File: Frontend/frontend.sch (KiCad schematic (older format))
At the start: 13 parts, among them J1 VOCM, J2 BNC, J3 UMC, J4 UMC, J5 VOCM, J6 BNC, J7 UMC, J8 UMC, J9 PCIEx4 EDGE

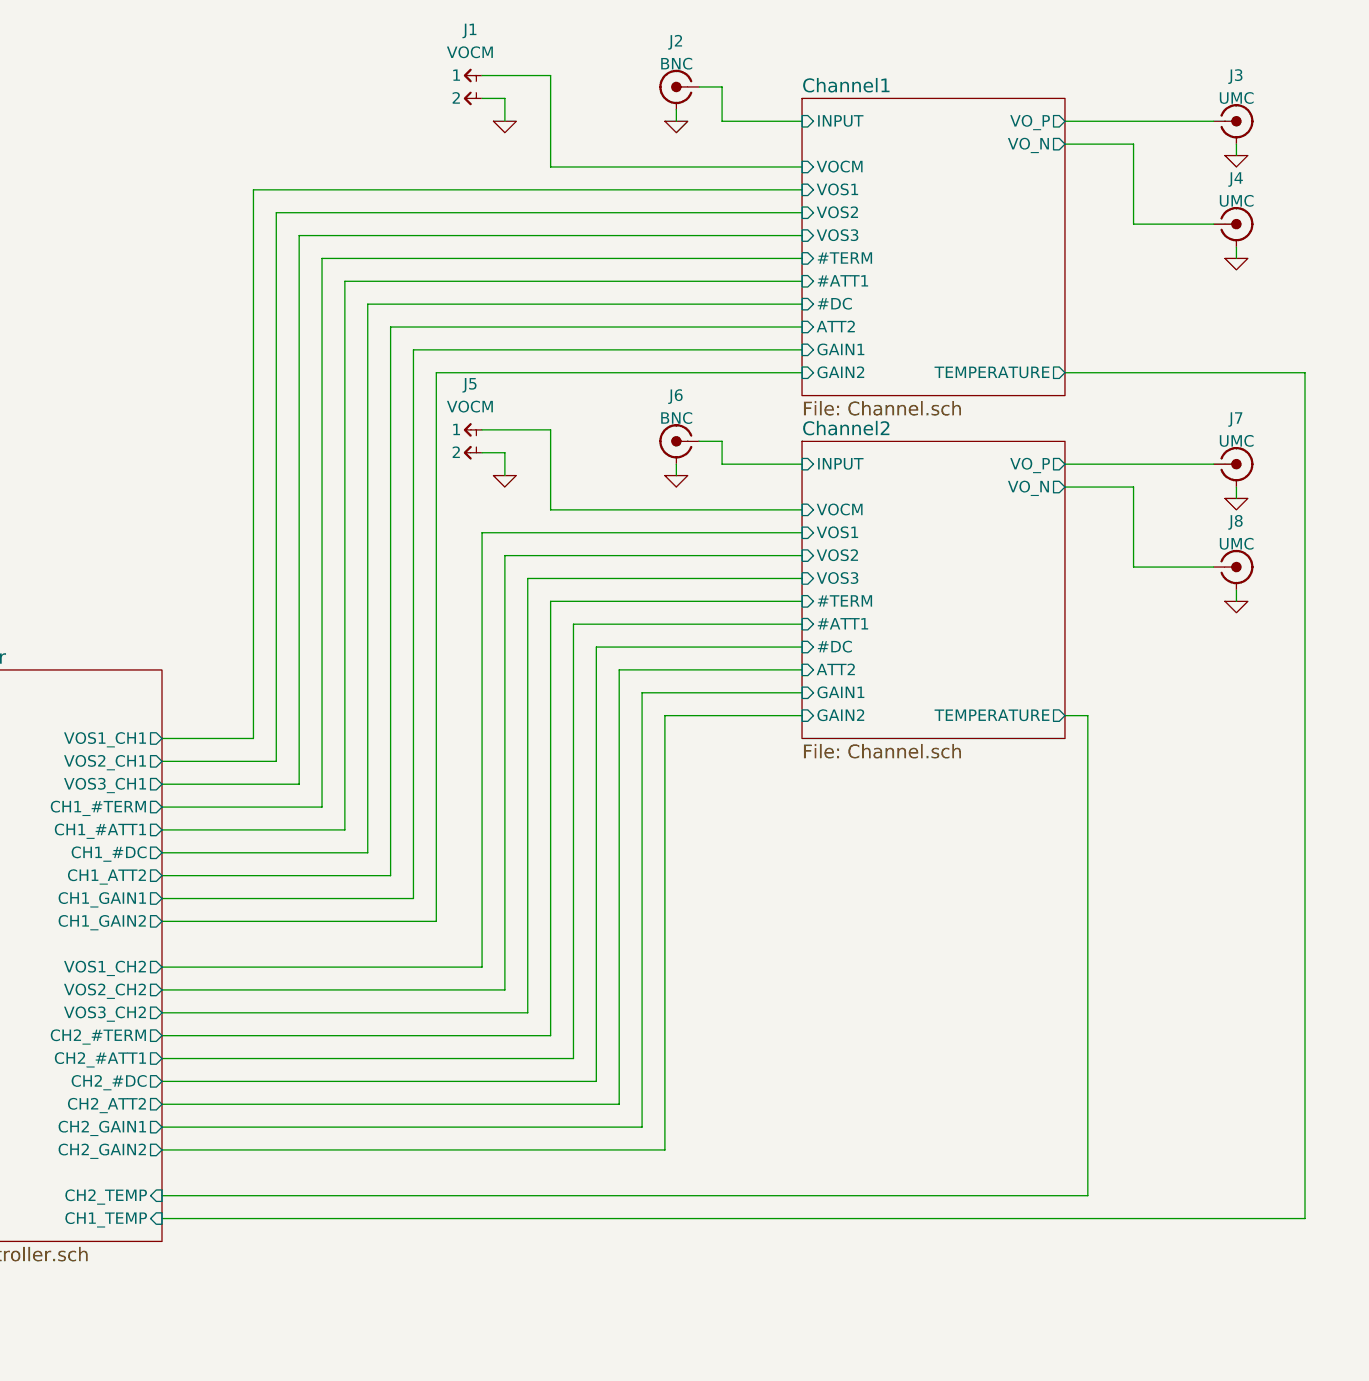
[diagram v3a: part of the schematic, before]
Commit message: Switch acq connectors to SATA
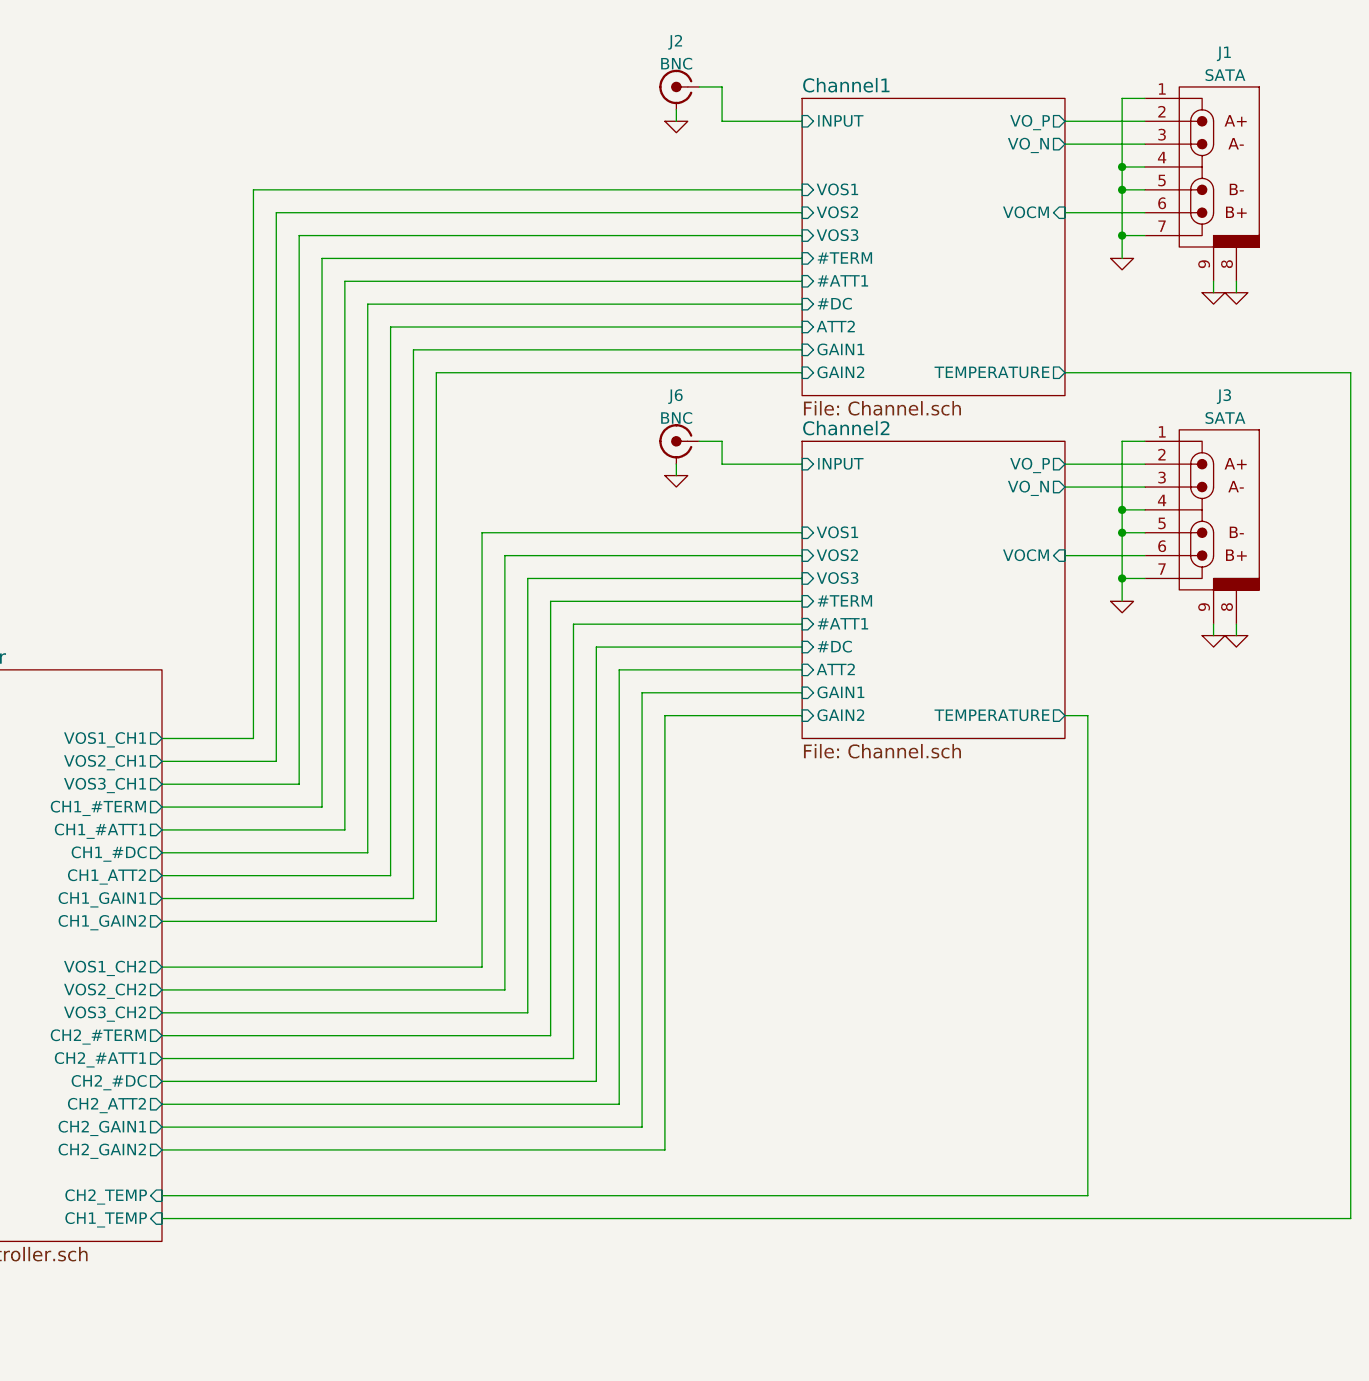
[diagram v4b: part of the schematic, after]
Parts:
- removed J1, J5: VOCM, conn-100mil:CONN-100MIL-M-1x2, symbol CONN-100MIL-M-1x2
- removed J3, J4, J7, J8: UMC, conn-molex:CONN-MOLEX-0734120110, symbol CONN-MOLEX-0734120110
- added J1, J3: SATA, conn-molex:CONN-MOLEX-0678005001, symbol CONN-MOLEX-0678005001
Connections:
- net Channel1/VOCM: now also J1.6 (A-)
- net Channel1/VO_N: now also J1.3 (A-)
- net Channel1/VO_P: now also J1.2 (A+)
- net Channel2/VOCM: now also J3.6 (A-)
- net Channel2/VO_N: now also J3.3 (A-)
- net Channel2/VO_P: now also J3.2 (A+)
- net GND: now also J1.1 (GND), J1.4, J1.5 (A+), J1.7 (GND), J1.8, J1.9, J3.1 (GND), J3.4, J3.5 (A+), J3.7 (GND), J3.8, J3.9

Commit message: More routing adjustments
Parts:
- added DZ2: 40V, symbol ZENER
- added K7: RELAY_DPDT, symbol RELAY_DPDT
- added Q2: NPNDARL2, symbol NPNDARL2
- added R129: R, symbol R
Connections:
- net +12: now also K7.CP
- net GND: now also DZ2.A, Q2.E
- new net: Q2.B, R129.1
- new net: DZ2.K, K7.CN, Q2.C

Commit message: Finally finish the final layout finally
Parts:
- removed DZ2: 40V, symbol ZENER
- removed K7: RELAY_DPDT, symbol RELAY_DPDT
- removed Q2: NPNDARL2, symbol NPNDARL2
- removed R129: R, symbol R
- J1, J3: BOM (none) -> DIST DIGIKEY WM3467-ND
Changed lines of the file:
@@
 F 2 "conn-molex:CONN-MOLEX-0678005001" H 9750 1500 50  0001 C CNN
 F 3 "" H 9850 1650 50  0000 C CNN
+F 4 "DIST DIGIKEY WM3467-ND" H 9750 1500 60  0001 C CNN "BOM"
 	1    9750 1500
 	-1   0    0    -1
@@
 F 2 "conn-molex:CONN-MOLEX-0678005001" H 9750 3000 50  0001 C CNN
 F 3 "" H 9850 3150 50  0000 C CNN
+F 4 "DIST DIGIKEY WM3467-ND" H 9750 3000 60  0001 C CNN "BOM"
 	1    9750 3000
 	-1   0    0    -1
@@
 	1    0    0    -1
 $EndComp
-$Comp
-L NPNDARL2 Q2
-U 1 1 556552E7
-P 5750 -300
-F 0 "Q2" H 5700 -150 50  0000 C CNN
-F 1 "NPNDARL2" H 6000 -350 50  0001 C CNN
-F 2 "" H 5750 -300 60  0000 C CNN
-F 3 "" H 5750 -300 60  0000 C CNN
-	1    5750 -300
-	1    0    0    -1
-$EndComp
-$Comp
-L RELAY_DPDT K7
-U 3 1 55655FEE
-P 5800 -650
-F 0 "K7" V 5700 -750 50  0000 C CNN
-F 1 "RELAY_DPDT" H 5800 -750 50  0001 C CNN
-F 2 "" H 5800 -650 60  0000 C CNN
-F 3 "" H 5800 -650 60  0000 C CNN
-	3    5800 -650
-	0    1    1    0
-$EndComp
-$Comp
-L ZENER DZ2
-U 1 1 55657226
-P 5950 -300
-F 0 "DZ2" H 6100 -250 50  0000 C CNN
-F 1 "40V" H 6100 -350 50  0000 C CNN
-F 2 "" H 5950 -300 60  0000 C CNN
-F 3 "" H 5950 -300 60  0000 C CNN
-	1    5950 -300
-	1    0    0    -1
-$EndComp
-$Comp
-L GND #PWR023
-U 1 1 556576C0
-P 5800 -100
-F 0 "#PWR023" H 5800 -100 30  0001 C CNN
-F 1 "GND" H 5800 -170 30  0001 C CNN
-F 2 "" H 5800 -100 60  0000 C CNN
-F 3 "" H 5800 -100 60  0000 C CNN
-	1    5800 -100
-	1    0    0    -1
-$EndComp
 Wire Wire Line
 	2400 3900 2900 3900
@@
 Wire Wire Line
 	9800 3550 9800 3500
-Wire Wire Line
-	5800 -550 5800 -400
-Wire Wire Line
-	5800 -750 5800 -850
-Wire Wire Line
-	5800 -450 5950 -450
-Wire Wire Line
-	5950 -450 5950 -400
-Connection ~ 5800 -450
-Wire Wire Line
-	5800 -200 5800 -100
-Wire Wire Line
-	5800 -150 5950 -150
-Wire Wire Line
-	5950 -150 5950 -200
-Connection ~ 5800 -150
-$Comp
-L R R129
-U 1 1 55658540
-P 5450 -300
-F 0 "R129" V 5350 -300 50  0000 C CNN
-F 1 "R" H 5600 -350 50  0001 C CNN
-F 2 "" H 5450 -250 60  0000 C CNN
-F 3 "" H 5450 -250 60  0000 C CNN
-	1    5450 -300
-	0    1    1    0
-$EndComp
-Wire Wire Line
-	5550 -300 5650 -300
-$Comp
-L +12 #PWR024
-U 1 1 55658D52
-P 5800 -850
-F 0 "#PWR024" H 5800 -800 30  0001 C CNN
-F 1 "+12" H 5800 -750 50  0000 C CNN
-F 2 "" H 5800 -850 60  0000 C CNN
-F 3 "" H 5800 -850 60  0000 C CNN
-	1    5800 -850
-	1    0    0    -1
-$EndComp
 $EndSCHEMATC
